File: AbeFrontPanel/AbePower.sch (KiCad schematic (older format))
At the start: 62 parts

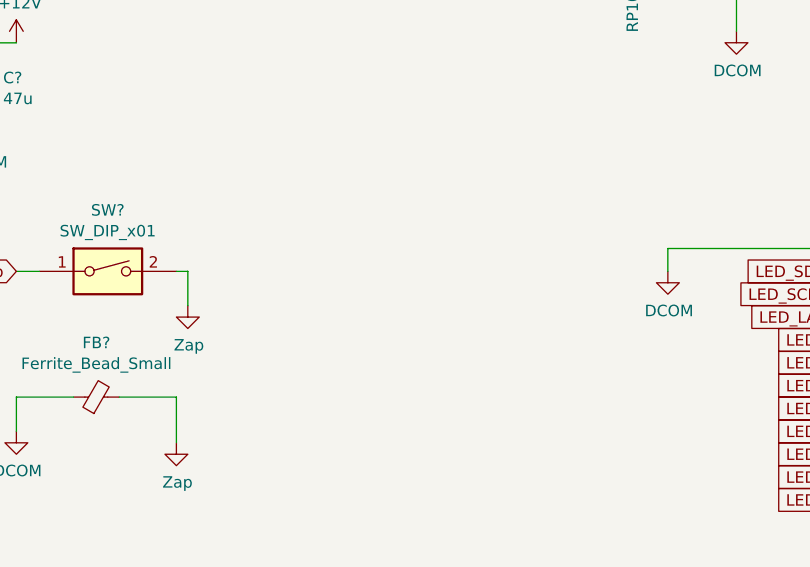
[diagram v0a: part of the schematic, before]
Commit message: Add TLV1117 Adjustable Regulator
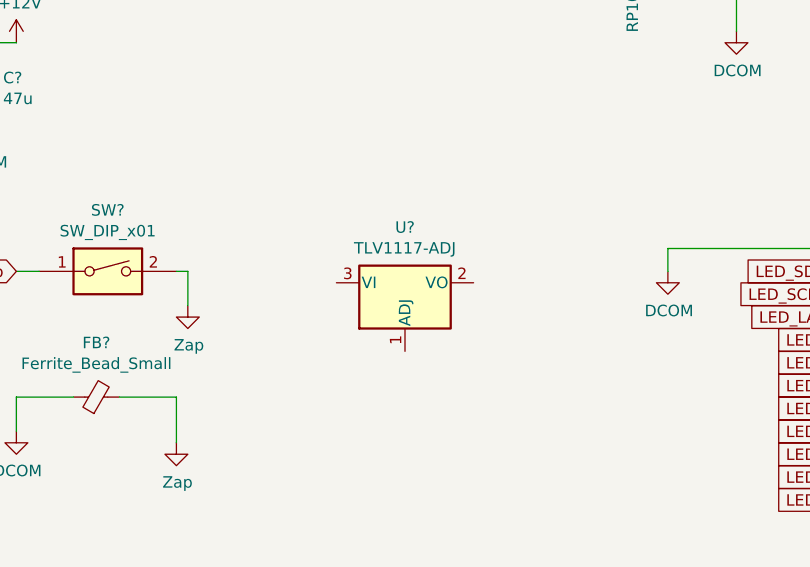
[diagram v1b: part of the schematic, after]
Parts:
- added U?: TLV1117-ADJ, symbol Regulator_Linear:TLV1117-ADJ
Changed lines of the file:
@@
 	0    -1   -1   0
 $EndComp
+$Comp
+L Regulator_Linear:TLV1117-ADJ U?
+U 1 1 608AAEB4
+P 4950 3050
+F 0 "U?" H 4950 3292 50  0000 C CNN
+F 1 "TLV1117-ADJ" H 4950 3201 50  0000 C CNN
+F 2 "" H 4950 3050 50  0001 C CNN
+F 3 "http://www.ti.com/lit/ds/symlink/tlv1117.pdf" H 4950 3050 50  0001 C CNN
+	1    4950 3050
+	1    0    0    -1
+$EndComp
 $EndSCHEMATC

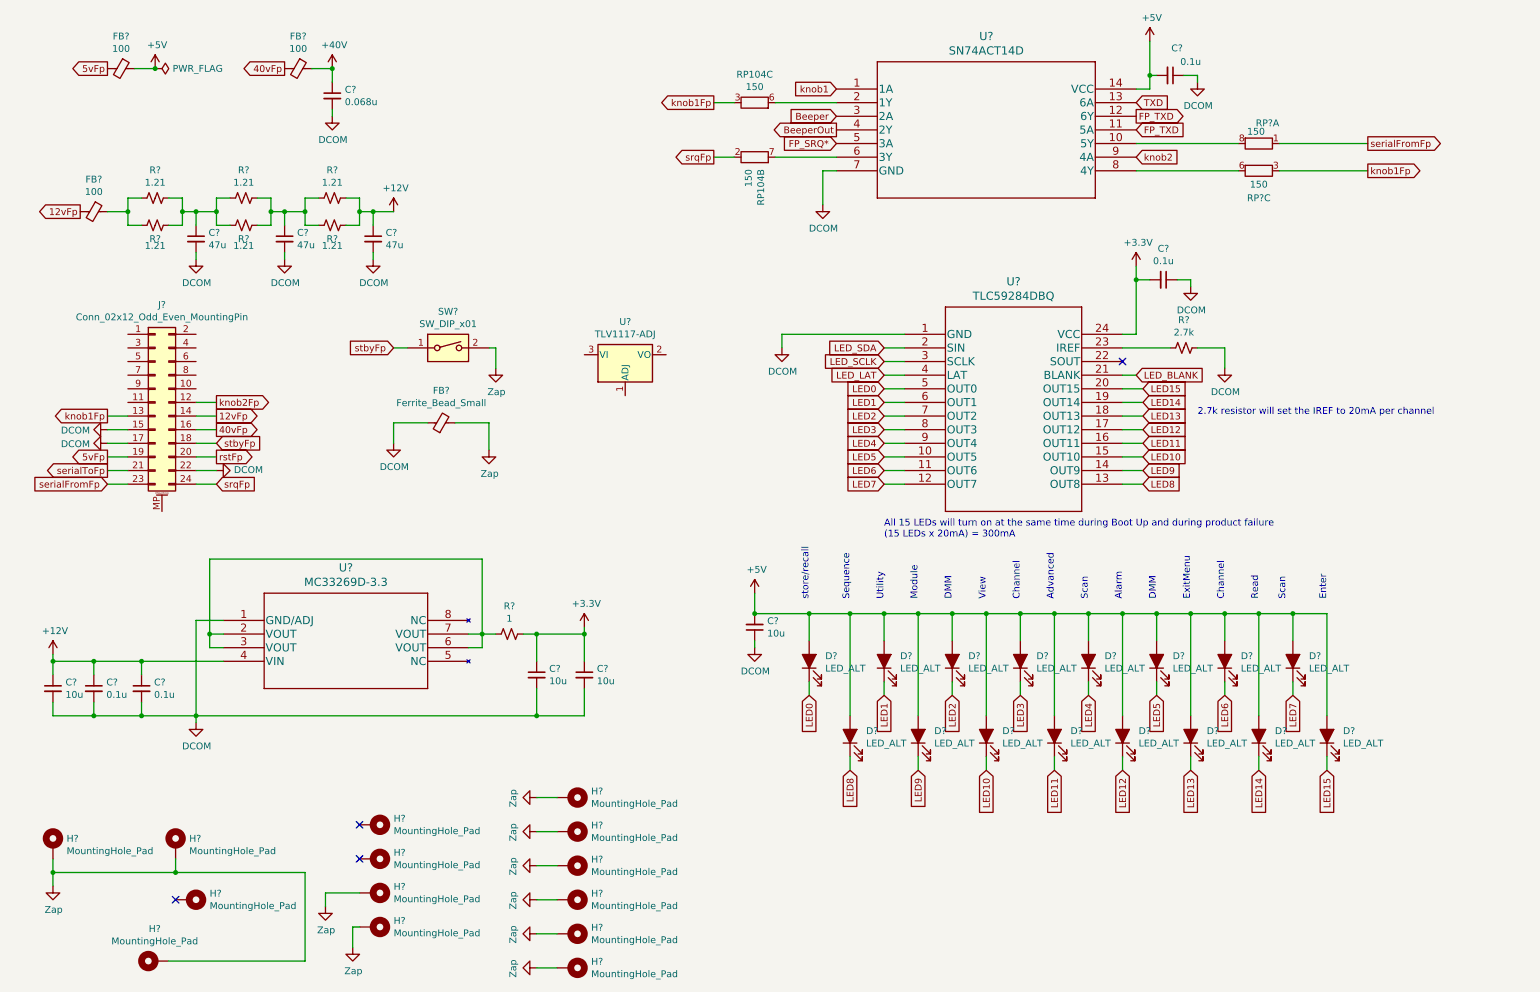
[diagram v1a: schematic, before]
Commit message: +10V, Beeper
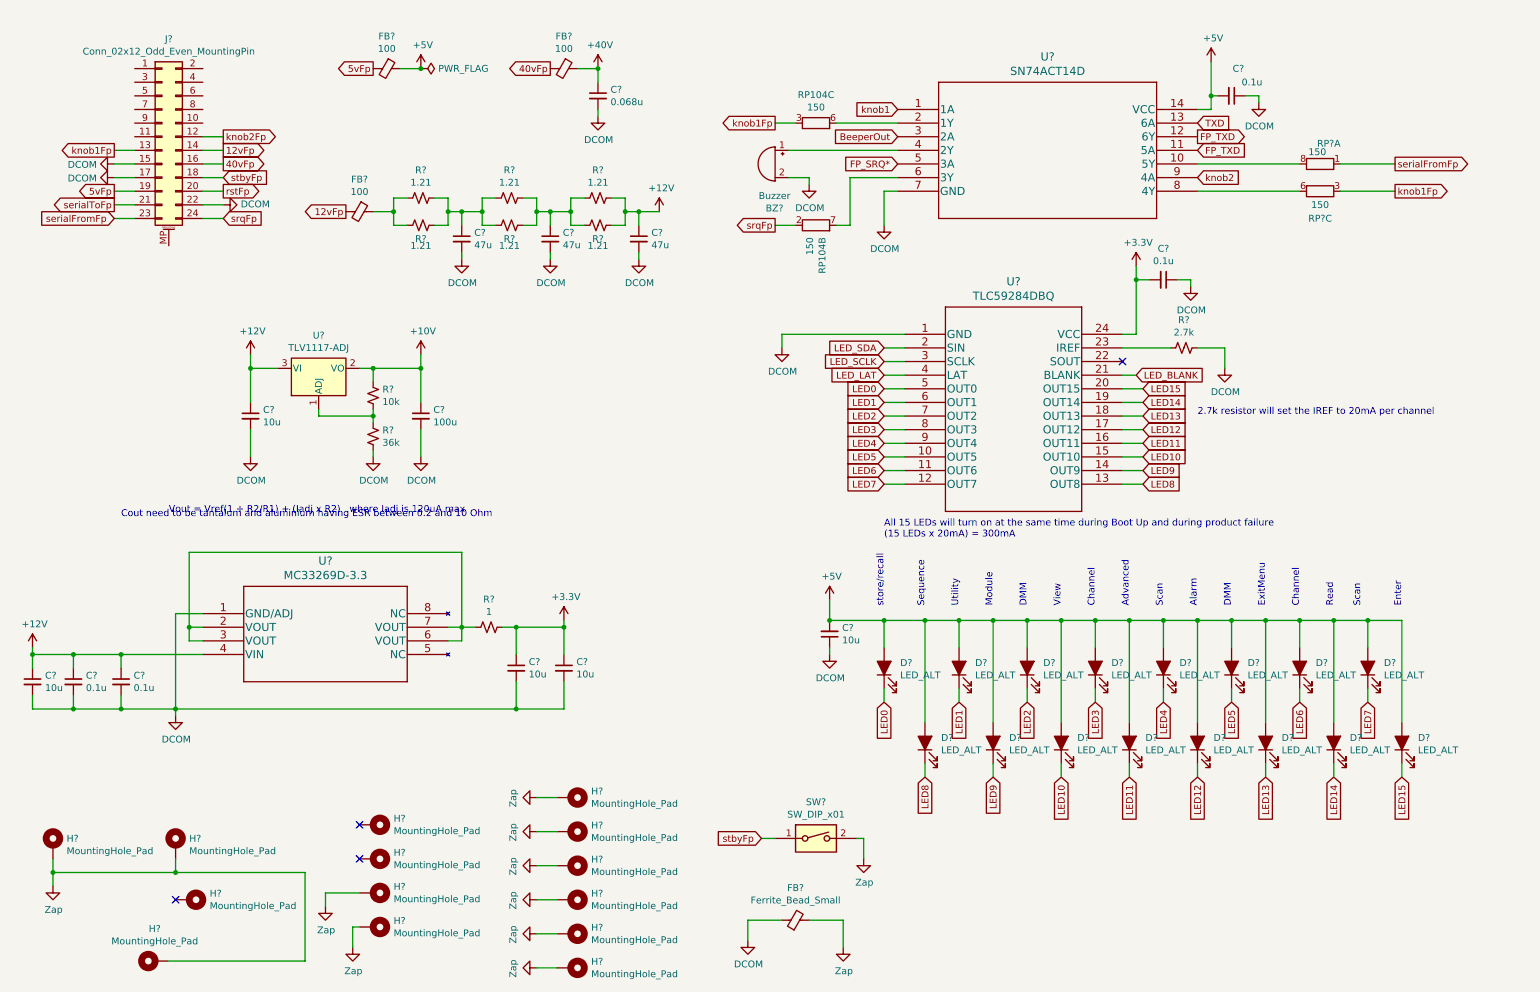
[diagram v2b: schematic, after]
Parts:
- added BZ?: Buzzer, symbol Device:Buzzer
- added C?: 10u, symbol Device:C_Small
- added C?: 100u, symbol Device:C_Small
- added R?: 10k, symbol Device:R_Small_US
- added R?: 36k, symbol Device:R_Small_US
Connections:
- net Beeper is gone; now on net BeeperOut: U?.3 (2A)
- net +12V: now also U?.3 (VI), C?.1
- net BeeperOut: no longer U?.4 (2Y)
- net GND: now also BZ?.2 (+), C?.2, C?.2, R?.2
- net at U?.1 (ADJ): now also R?.1, R?.2
- net +10V: now reaches U?.2 (VO)
- net +10V: now also C?.1, R?.1
- new net: BZ?.1 (-), U?.4 (2Y)
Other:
- note added: "Cout need to be tantalum and aluminium having ESR between 0.2 and 10 Ohm"
- note added: "Vout = Vref(1 + R2/R1) + (Iadj x R2) where Iadj is 120uA max\n\n"
- moved on the sheet: C?, D?, FB?, J?, R?, RP104B, RP104C, RP?A, RP?C, SW?, U?

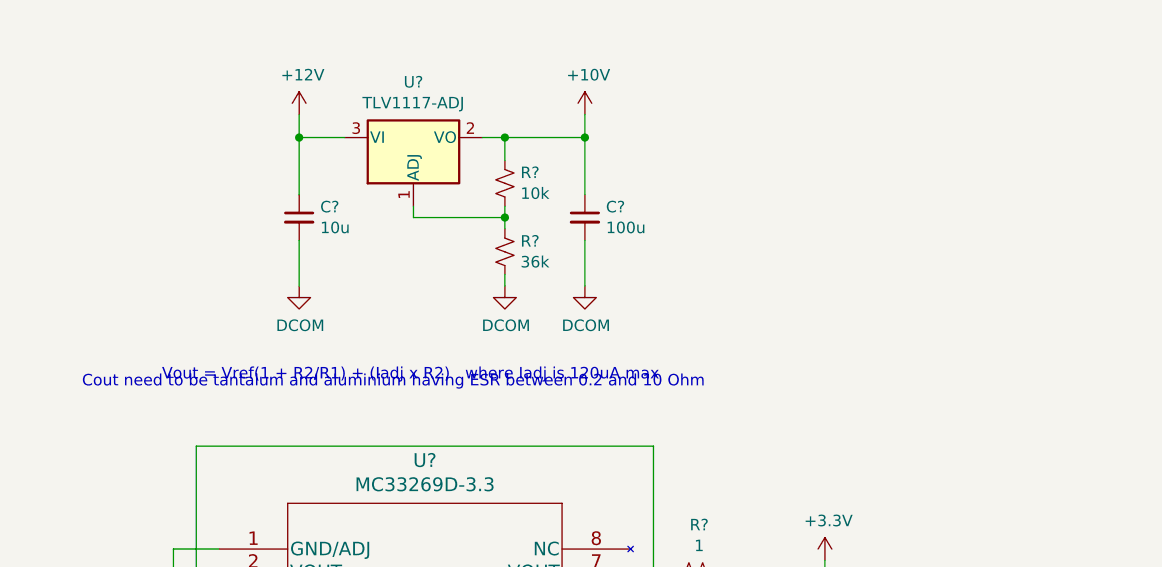
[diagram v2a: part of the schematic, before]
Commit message: Change the value of TL1117 R2/R1 to lower value
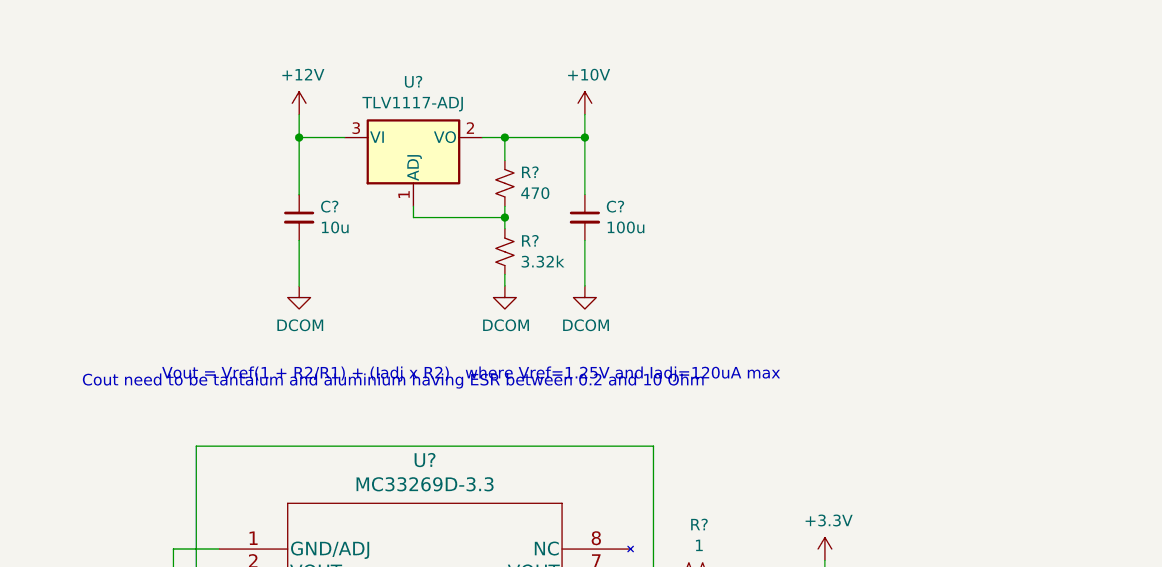
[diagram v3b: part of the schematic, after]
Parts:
- R?: value 10k -> 470
- R?: value 36k -> 3.32k
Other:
- note added: "Vout = Vref(1 + R2/R1) + (Iadj x R2) where Vref=1.25V and Iadj=120uA max\n\n"
- note removed: "Vout = Vref(1 + R2/R1) + (Iadj x R2) where Iadj is 120uA max\n\n"
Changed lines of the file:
@@
 P 3100 3350
 F 0 "R?" H 3168 3396 50  0000 L CNN
-F 1 "10k" H 3168 3305 50  0000 L CNN
+F 1 "470" H 3168 3305 50  0000 L CNN
 F 2 "" H 3100 3350 50  0001 C CNN
 F 3 "~" H 3100 3350 50  0001 C CNN
@@
 P 3100 3650
 F 0 "R?" H 3168 3696 50  0000 L CNN
-F 1 "36k" H 3168 3605 50  0000 L CNN
+F 1 "3.32k" H 3168 3605 50  0000 L CNN
 F 2 "" H 3100 3650 50  0001 C CNN
 F 3 "~" H 3100 3650 50  0001 C CNN
@@
 	3450 3050 3450 3150
 Connection ~ 3450 3150
-Text Notes 1600 4300 0    50   ~ 0
-Vout = Vref(1 + R2/R1) + (Iadj x R2)   where Iadj is 120uA max\n\n
 Text Notes 1250 4250 0    50   ~ 0
 Cout need to be tantalum and aluminium having ESR between 0.2 and 10 Ohm
@@
 Wire Wire Line
 	6300 1750 6300 1800
+Text Notes 1600 4300 0    50   ~ 0
+Vout = Vref(1 + R2/R1) + (Iadj x R2)   where Vref=1.25V and Iadj=120uA max\n\n
 $EndSCHEMATC

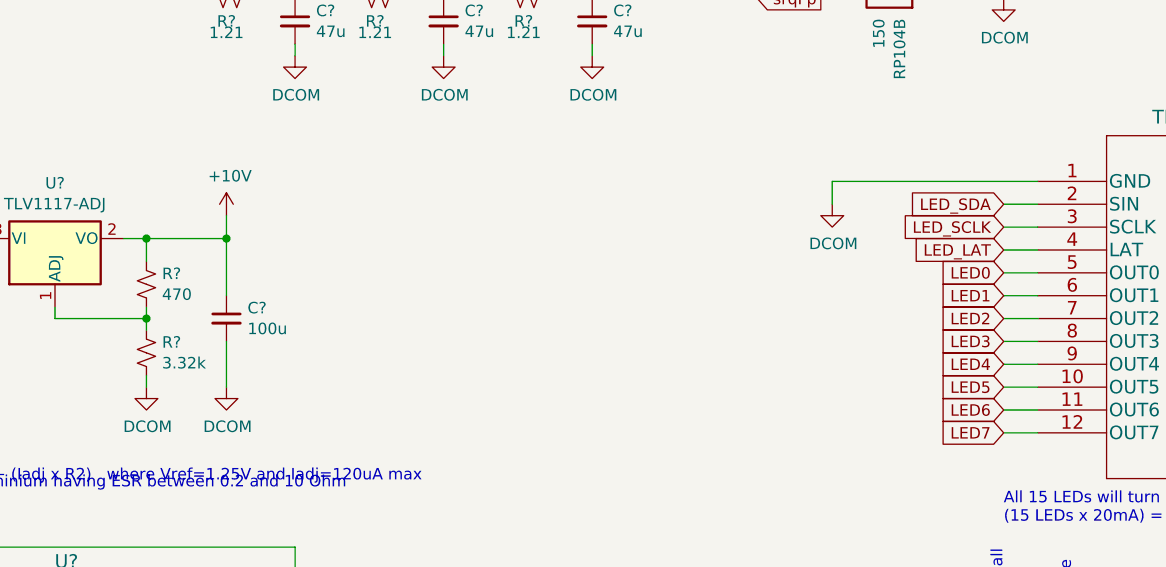
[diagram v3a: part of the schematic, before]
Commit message: Revise the value of TLV1117 R2/R1. Changed LED_SDA to LED_MOSI
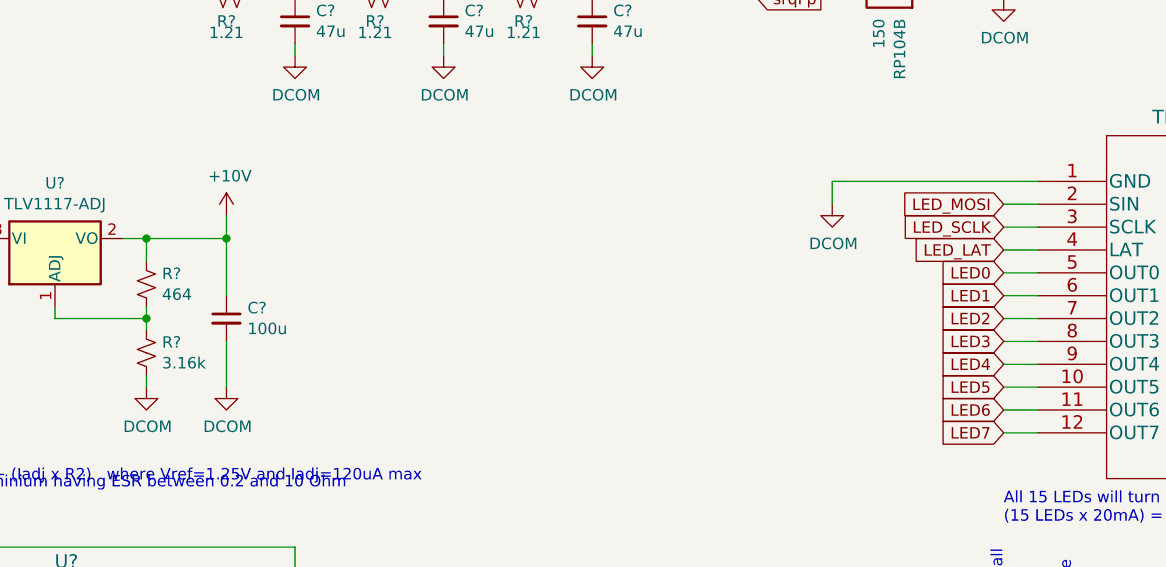
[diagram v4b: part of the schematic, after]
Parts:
- R?: value 470 -> 464
- R?: value 3.32k -> 3.16k
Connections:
- net LED_SDA renamed LED_MOSI
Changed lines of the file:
@@
 NoConn ~ 8600 3100
 Text GLabel 6850 3000 0    50   Input ~ 0
-LED_SDA
+LED_MOSI
 Wire Wire Line
 	6850 3000 7000 3000
@@
 P 3100 3350
 F 0 "R?" H 3168 3396 50  0000 L CNN
-F 1 "470" H 3168 3305 50  0000 L CNN
+F 1 "464" H 3168 3305 50  0000 L CNN
 F 2 "" H 3100 3350 50  0001 C CNN
 F 3 "~" H 3100 3350 50  0001 C CNN
@@
 P 3100 3650
 F 0 "R?" H 3168 3696 50  0000 L CNN
-F 1 "3.32k" H 3168 3605 50  0000 L CNN
+F 1 "3.16k" H 3168 3605 50  0000 L CNN
 F 2 "" H 3100 3650 50  0001 C CNN
 F 3 "~" H 3100 3650 50  0001 C CNN

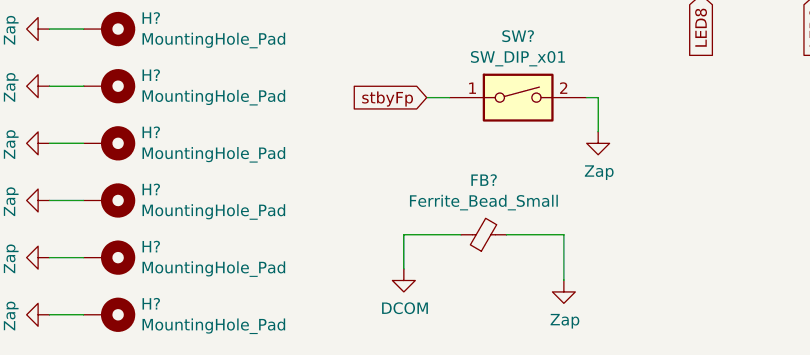
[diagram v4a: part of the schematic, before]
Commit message: Add RC time constant to slow down FilLogic. Add DRV8210 symbol.
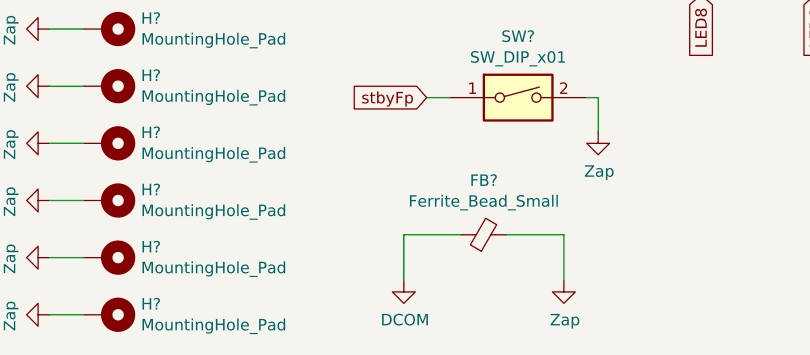
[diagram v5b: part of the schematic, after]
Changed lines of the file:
@@
 L power:DCOM #PWR?
 U 1 1 609306B9
-P 5850 7350
-F 0 "#PWR?" H 5850 7100 50  0001 C CNN
-F 1 "DCOM" H 5855 7177 50  0000 C CNN
-F 2 "" H 5850 7350 50  0001 C CNN
-F 3 "" H 5850 7350 50  0001 C CNN
-	1    5850 7350
+P 5850 7400
+F 0 "#PWR?" H 5850 7150 50  0001 C CNN
+F 1 "DCOM" H 5855 7227 50  0000 C CNN
+F 2 "" H 5850 7400 50  0001 C CNN
+F 3 "" H 5850 7400 50  0001 C CNN
+	1    5850 7400
 	1    0    0    -1
 $EndComp
@@
 $EndComp
 Wire Wire Line
-	5850 7350 5850 7200
+	5850 7400 5850 7200
 Wire Wire Line
 	5850 7200 6100 7200
